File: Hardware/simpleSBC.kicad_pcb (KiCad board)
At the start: 6 copper layers, 82.7 x 56 mm, 202 parts, among them J1 Conn_02x07_Odd_Even, J2 Micro_SD_Card_Det2, J3 Conn_02x10_Odd_Even, J4 Barrel_Jack_Switch, J5 USB_A, J6 USB_A, J7 RJ45_Wuerth_7499010121A, J8 Conn_01x03, J9 Conn_02x10_Odd_Even, SW1 SW_Push, U1 STM32MP157FAD1, U2 STMPS2252MTR, U3 MT41K256M16TW, U4 STPMIC1, U5 USBLC6-4SC6, U6 LAN8742A, X1 ASCO, Y1 32.786, Y3 24M

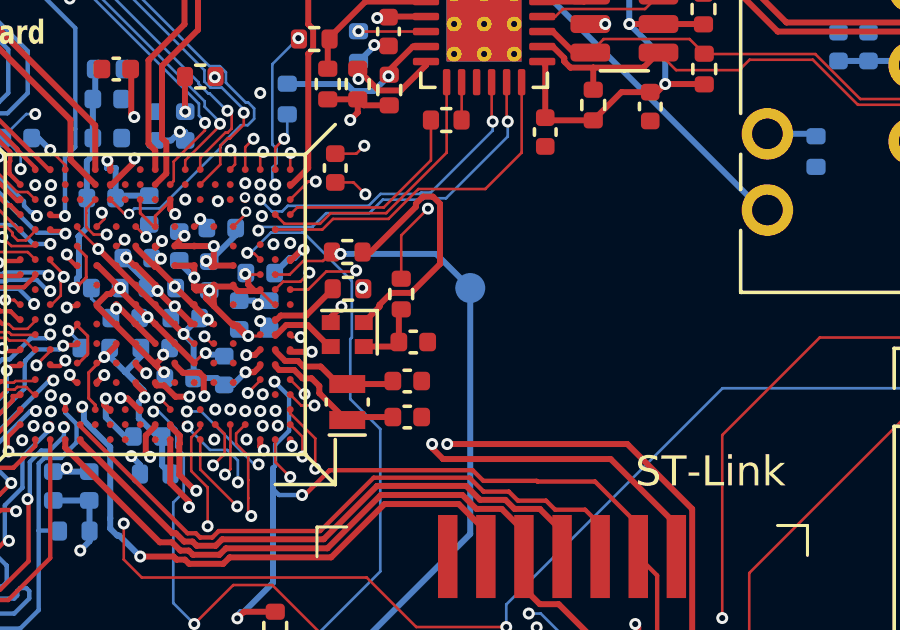
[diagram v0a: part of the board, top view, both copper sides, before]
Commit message: Add Boot selection jumpers
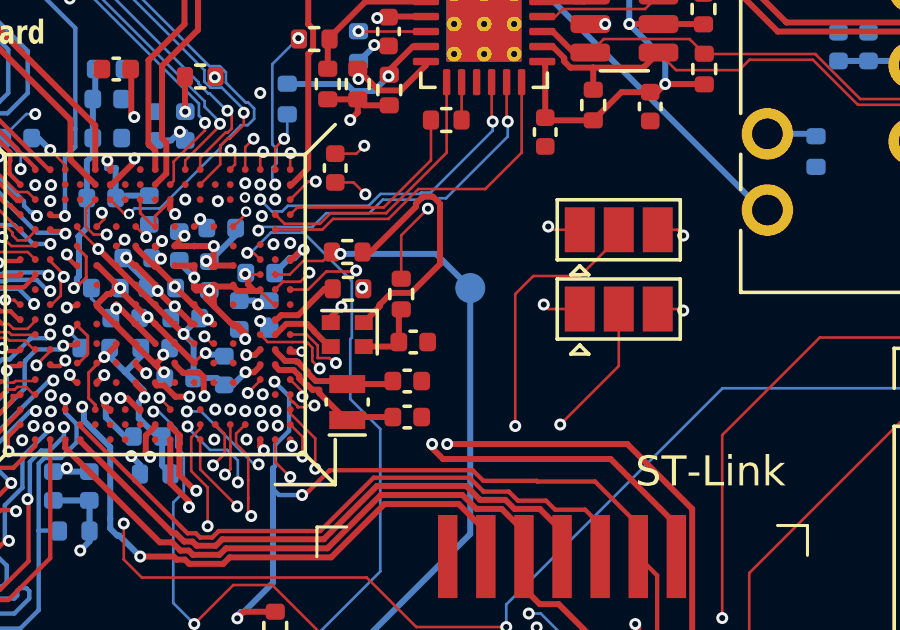
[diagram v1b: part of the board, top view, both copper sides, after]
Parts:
- added JP8: SolderJumper_3_Open, Jumper:SolderJumper-3_P1.3mm_Open_Pad1.0x1.5mm, F.Cu at (159.9, 83.4)
- added JP9: SolderJumper_3_Open, Jumper:SolderJumper-3_P1.3mm_Open_Pad1.0x1.5mm, F.Cu at (159.9, 86.0)
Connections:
- U1 pad H1: +3V3 -> Net-(JP8-C)
- U1 pad H3: +3V3 -> Net-(JP9-C)
- U1 pad U7: /PG10 -> unconnected-(U1B-PG10-PadU7)
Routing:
- net Net-(JP8-C): track 0.00 -> 18.9 mm, vias 0 -> 2
- net Net-(JP9-C): track 0.00 -> 17.4 mm, vias 0 -> 2
- net GND: track 214.1 -> 216.1 mm, vias 90 -> 92
- net +3V3: track 56.3 -> 57.2 mm, vias 29 -> 30

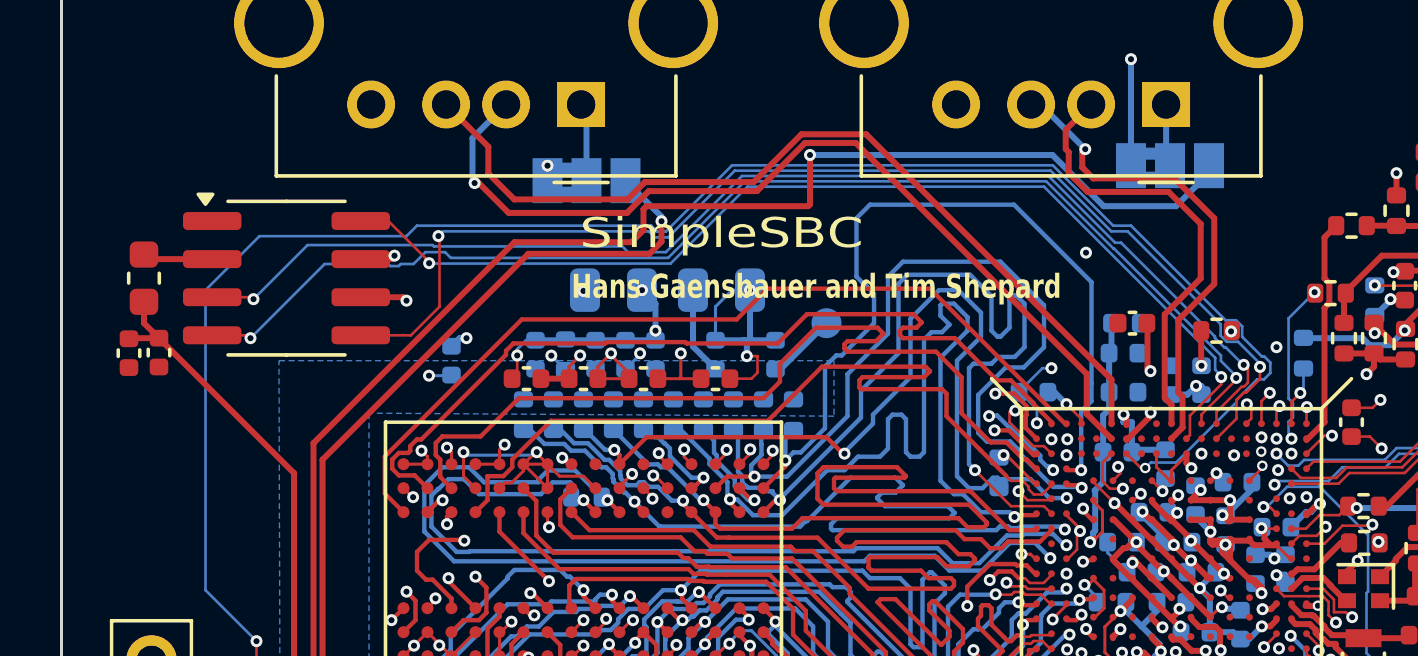
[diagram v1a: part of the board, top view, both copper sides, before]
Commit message: Add USB enable pulldowns
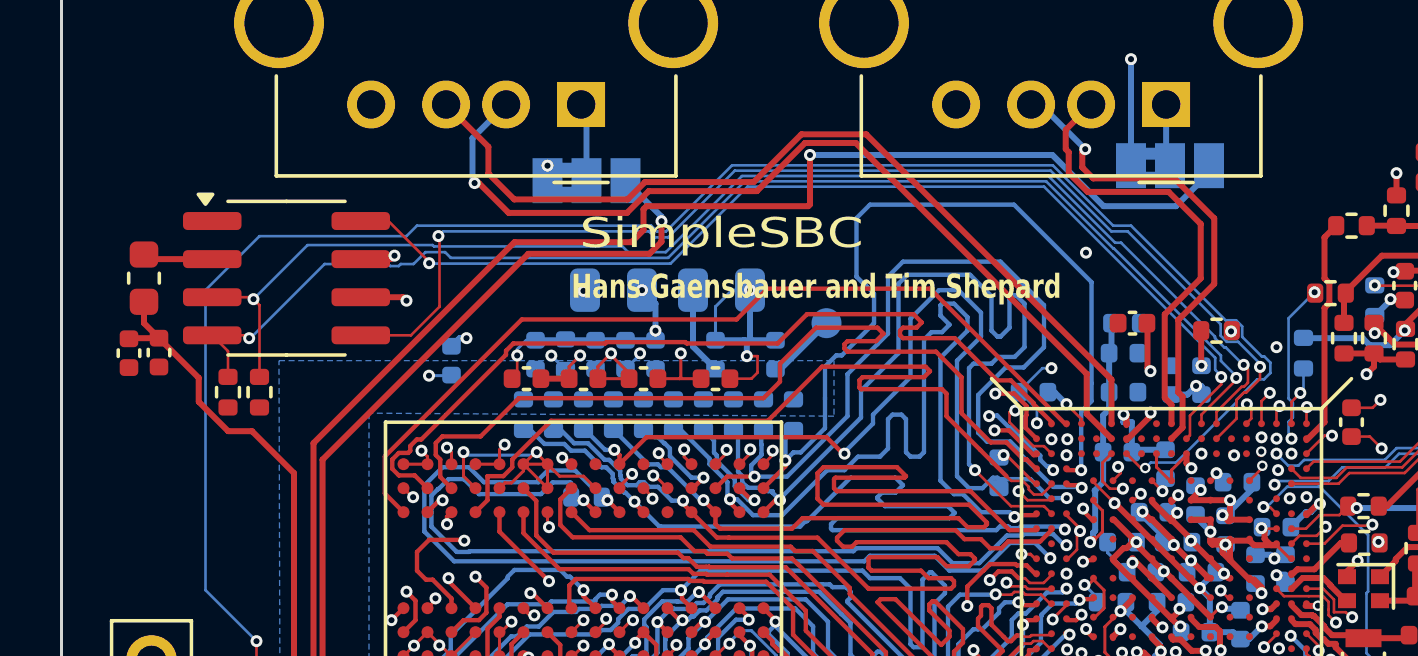
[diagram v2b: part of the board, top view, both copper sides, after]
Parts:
- added R59: 10k, Resistor_SMD:R_0402_1005Metric, F.Cu at (113.0, 80.3)
- added R64: 10k, Resistor_SMD:R_0402_1005Metric, F.Cu at (114.1, 80.3)
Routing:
- net /PRT1: track 41.4 -> 44.1 mm
- net /PRT2: track 41.4 -> 43.0 mm

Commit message: prepare for assembly
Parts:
- C36, C37: value 6.8n -> 10p
- C39, C41: value 47u -> 100n
- C42, C44: value 30p -> 10p
- C51: footprint Capacitor_SMD:C_0603_1608Metric -> Capacitor_SMD:C_0402_1005Metric
- C80: value 470p -> 220p
- R45, R50: value 270 -> 330
- R52, R53, R55, R56: value 51 -> 56
- U4: value STPMIC1 -> STPMIC1A
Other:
- board text added: "SimpleSBC V1"
- board text removed: "SimpleSBC"
